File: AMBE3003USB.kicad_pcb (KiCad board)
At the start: 2 copper layers, 72.6 x 71.6 mm, 101 parts, among them J1 McBSP, J2 ACONF, J3 CODEC, J4 USB_OTG, P1 CONFIG, U1 AMBE3003, U2 LD1117S33TR, U3 TPS3805, U4 FT232RL, U5 TPS78319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

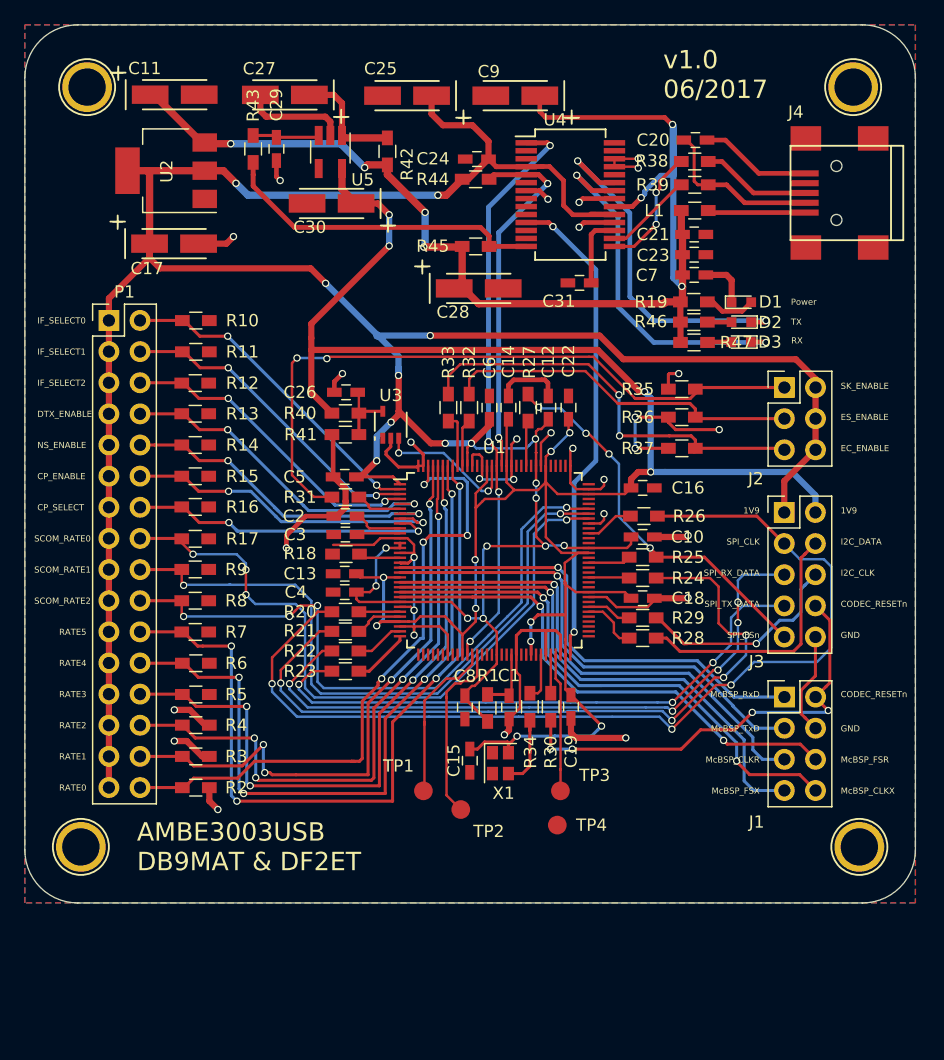
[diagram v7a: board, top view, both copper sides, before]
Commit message: Re-add OSH logo and TOP/BOT icons
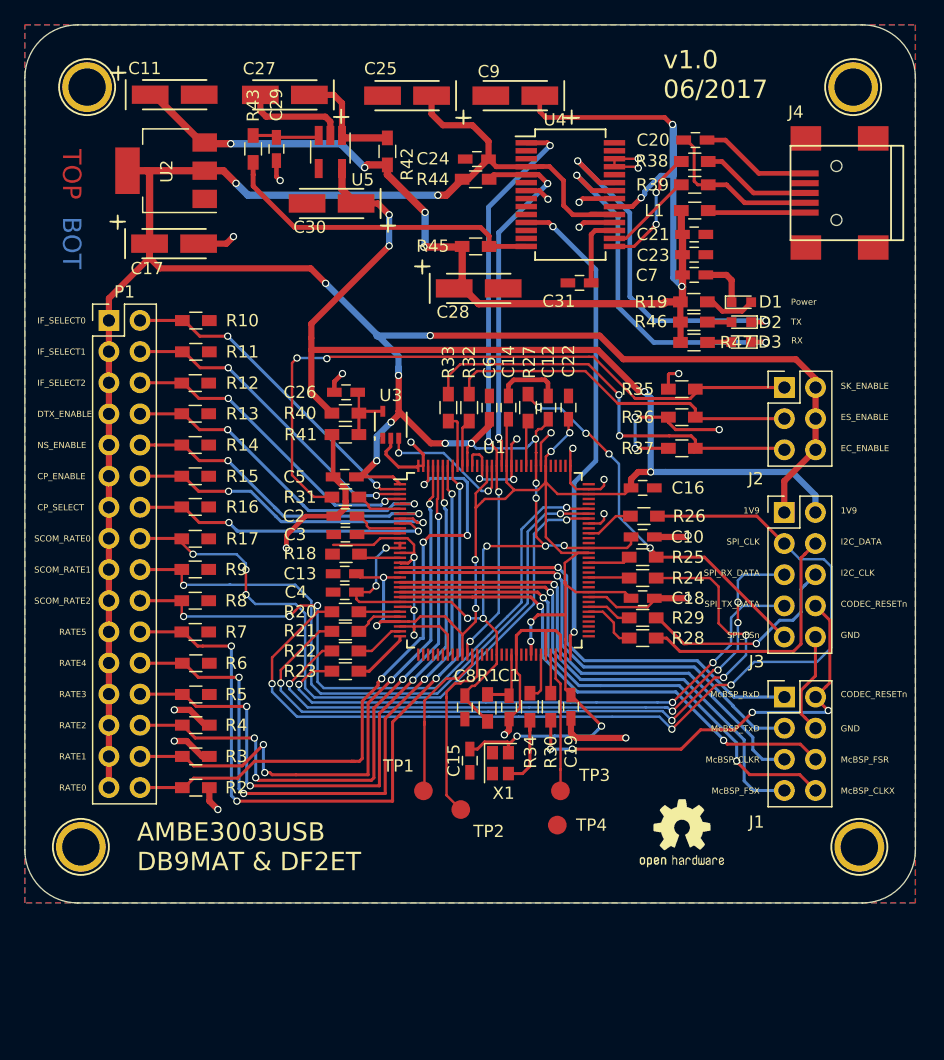
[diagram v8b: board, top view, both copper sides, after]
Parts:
- added G***: LOGO, OPENHARDWARE:OSHWLOGO0.3IN, F.Cu at (97.5, 111.5)
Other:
- net class Default: clearance 0.2 -> 0.3
- rule trace_clearance: 0.2 -> 0.3
- board text added: "BOT"
- board text added: "TOP"
